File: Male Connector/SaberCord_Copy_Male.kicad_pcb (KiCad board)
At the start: 2 copper layers, 29.8 x 20.3 mm, 6 parts, among them J1 Conn_02x07_Row_Letter_Last, J2 Conn_02x12_Row_Letter_Last

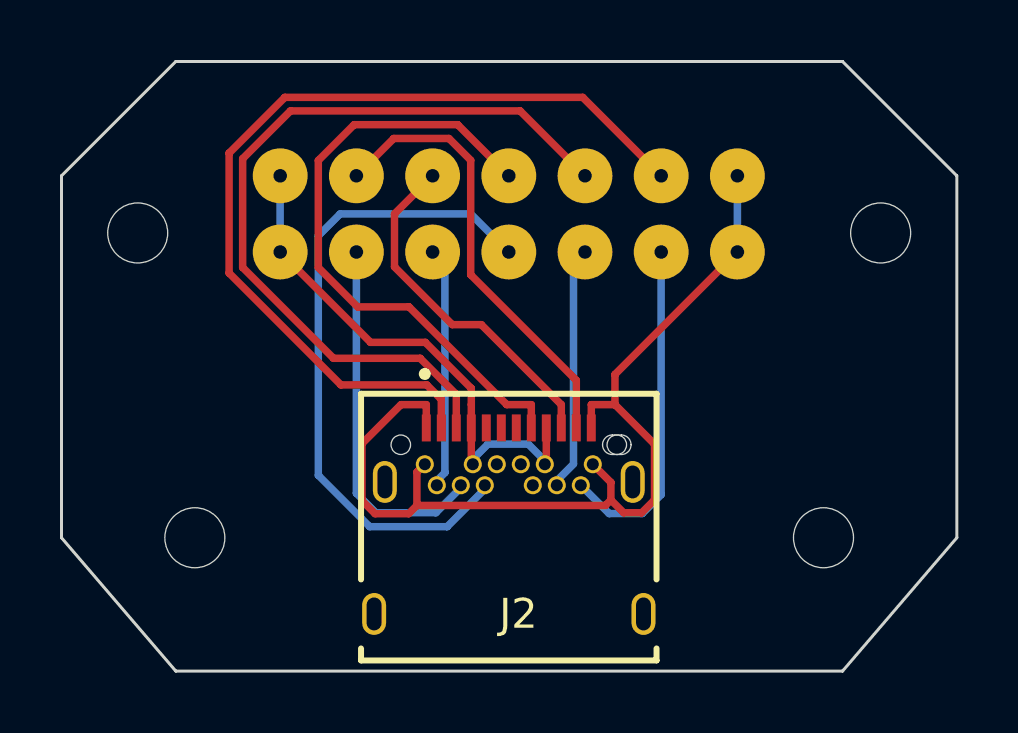
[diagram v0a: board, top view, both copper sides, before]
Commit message: flipped connector again, still incorrect fix later
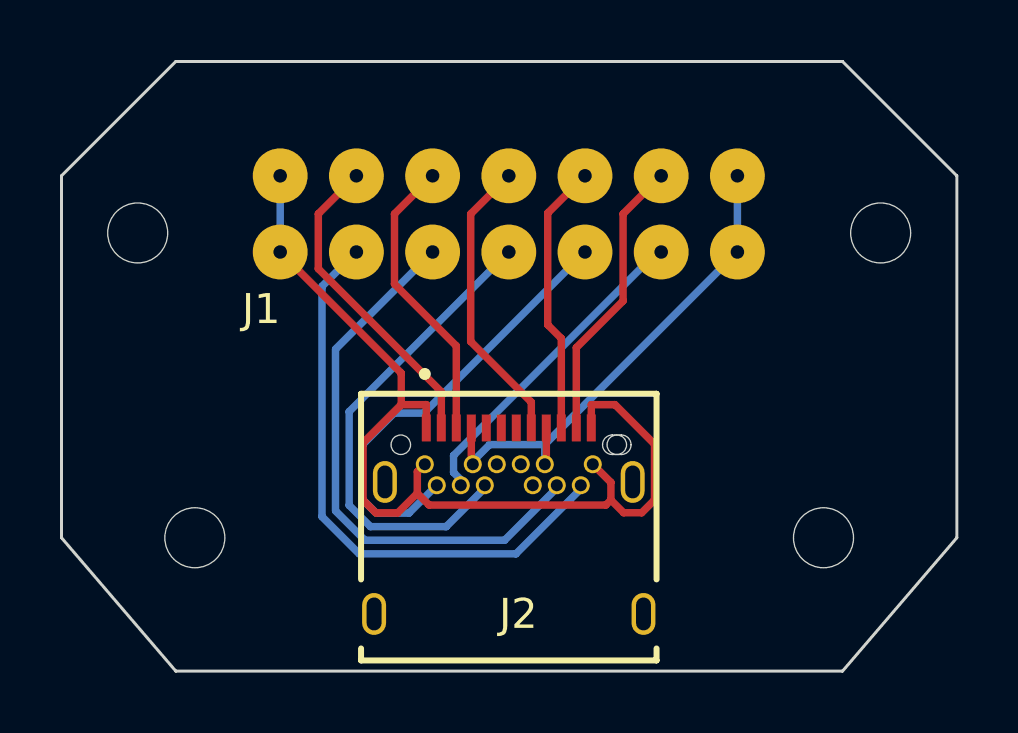
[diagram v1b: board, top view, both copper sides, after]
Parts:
- J1: moved to F.Cu
- turned J1 to 0 degrees
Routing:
- net /CAN0_H: track 30.0 -> 10.6 mm
- net /CAN0_L: track 26.6 -> 9.78 mm
- net /SBU1: track 20.9 -> 9.77 mm
- net /CAN2_L: track 8.16 -> 18.6 mm
- net /CAN2_H: track 11.4 -> 19.5 mm
- net /CAN3_H: track 8.06 -> 14.9 mm
- net /SBU2: track 22.1 -> 16.1 mm
- net /CAN1_H: track 15.0 -> 9.58 mm
- net /CAN1_L: track 11.8 -> 9.11 mm
- net /CAN3_L: track 12.2 -> 10.8 mm
